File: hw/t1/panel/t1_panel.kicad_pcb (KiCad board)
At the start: 4 copper layers, 70.5 x 81 mm, 391 parts, among them J1 SFP edge (INF-8074i), J2 Rosenberger E6S20A-40MT5-Z (H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, U1 DP83TG720S-Q1 (or DP83TC812S-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, U2 STM32G031F6P6, U3 TPS62822DLC, U4 TPS22918DBVR, Y1 25MHz CL8pF 2016

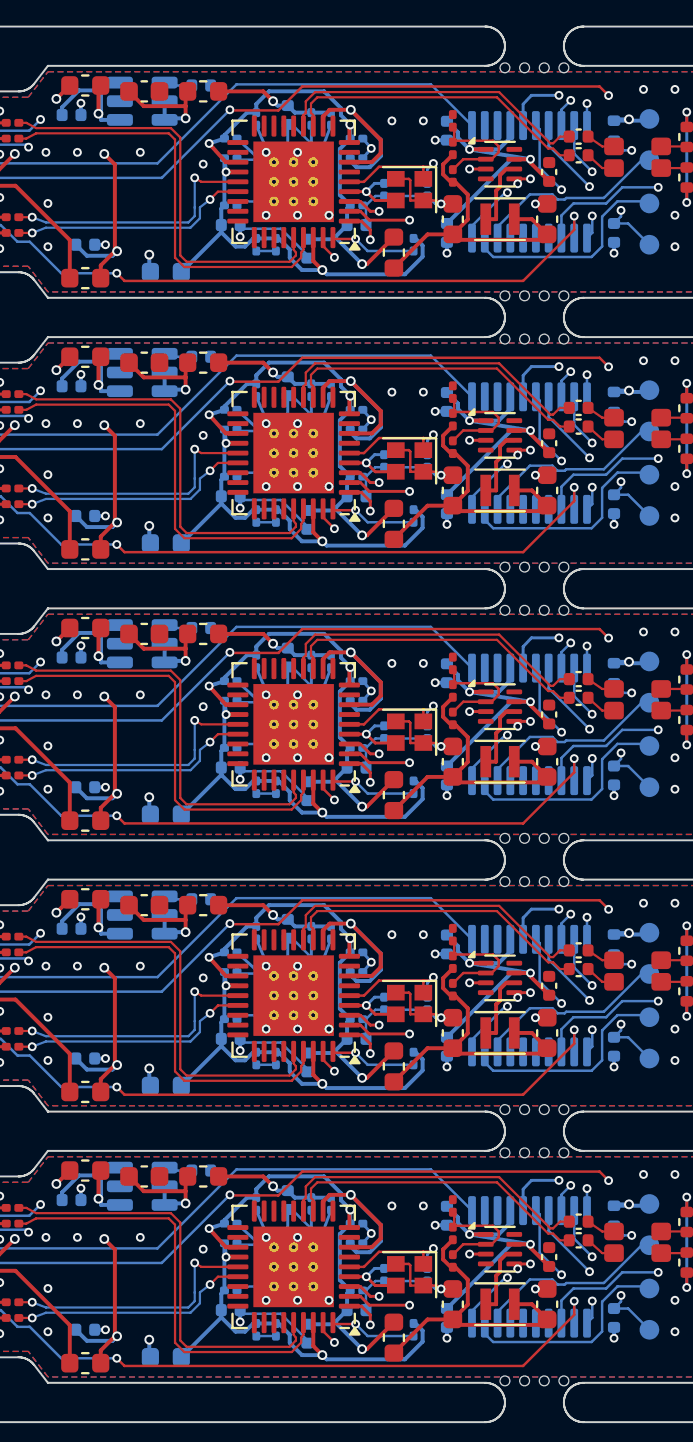
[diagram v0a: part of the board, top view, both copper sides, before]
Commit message: References checked against the design; the fixes they turned up
docs/REFERENCES.md: the standards, Linux drivers, TI / Realtek / Microchip /
Gowin datasheets, app notes and EVMs, and commercial modules, each with a
table of the design against it.

Fixed from it:
- T1S: CLKHOLD_N (K3) tied high - pulled down during configuration, it would
  have held the flash clock and the FPGA would never load; P1 (also
  SSPI_CS_N) pulled up (R26); AN1718 BIN: 0.75 W end-node resistors (were
  0.25 W), 100 V centre cap (was 50 V), no copper under the CMC
- RJ45 / T1S: buck inductor 1.0 uH (TPS6282x Table 3): the RTL8221B wants
  its core switcher out of pulse skipping, which now starts at ~0.15 A, not
  ~0.33 A
- T1: no copper under the CMC on F/In1 (DP83TG720 8.5); the TC812 loadout
  fits the 200 uH CMC its datasheet asks for
- fw: PHY settings 70 ms after reset release (TG720: 65 ms before the first
  MDIO frame) with the 0x56 bridge answering 0xFFFF until then; LAN8670 set-up
  picked by silicon revision (AN1699 Rev G: C2 or D0); collision detection
  follows PLCA as AN1699 asks

All three boards: DRC 0 / 0 unconnected, KiCad 9 PASS, panels clean.
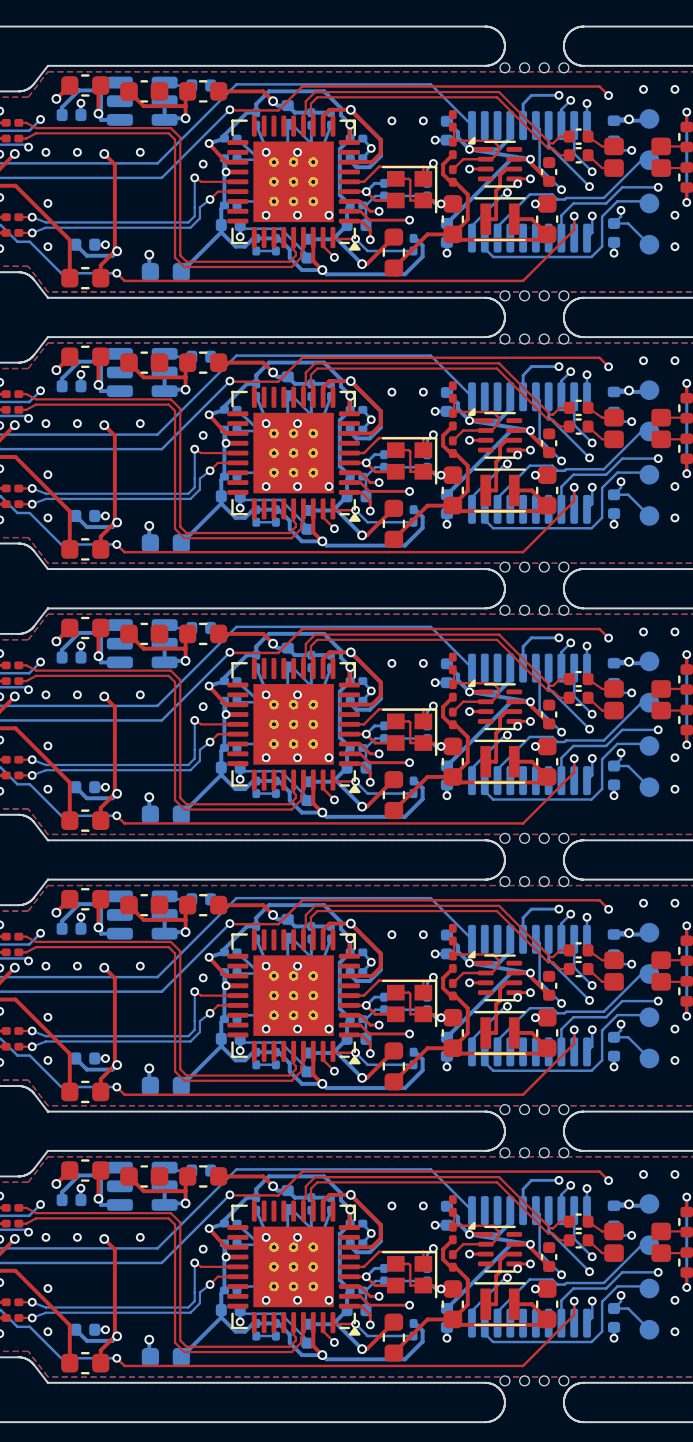
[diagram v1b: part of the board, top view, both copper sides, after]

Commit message: Review fixes: 100 V MDI DC block, 128 Mbit flash, T1S MDI geometry
- T1 C33/C34: 100 nF 100 V X5R 0402 (GRM155R62A104KE14D, C162178), split
  from the 16 V decap line (C1525) they had been grouped with
- T1 R6/R7: 1 k 1 % 0.2 W anti-surge 0402 (C313354) instead of 62.5 mW;
  still short of TI's 0.75 W 2010, documented
- T1S U2: GD25Q128EWIGR (C2982923), same WSON-8 footprint, so Gowin's
  default golden address 0x800000 is inside the part; ORDER.md gives the
  flash layout
- compliance.py: each lane's geometry comes from its routed track width;
  the T1S MDI is two 0.2 mm lines (Z0 44.8) with its own delay and loss,
  and an unsolved width now stops the run
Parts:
- C33 (x5), C34 (x5): value 100nF -> 100nF 100V
- R6 (x5), R7 (x5): value 1k 1% -> 1k 1% 0.2W

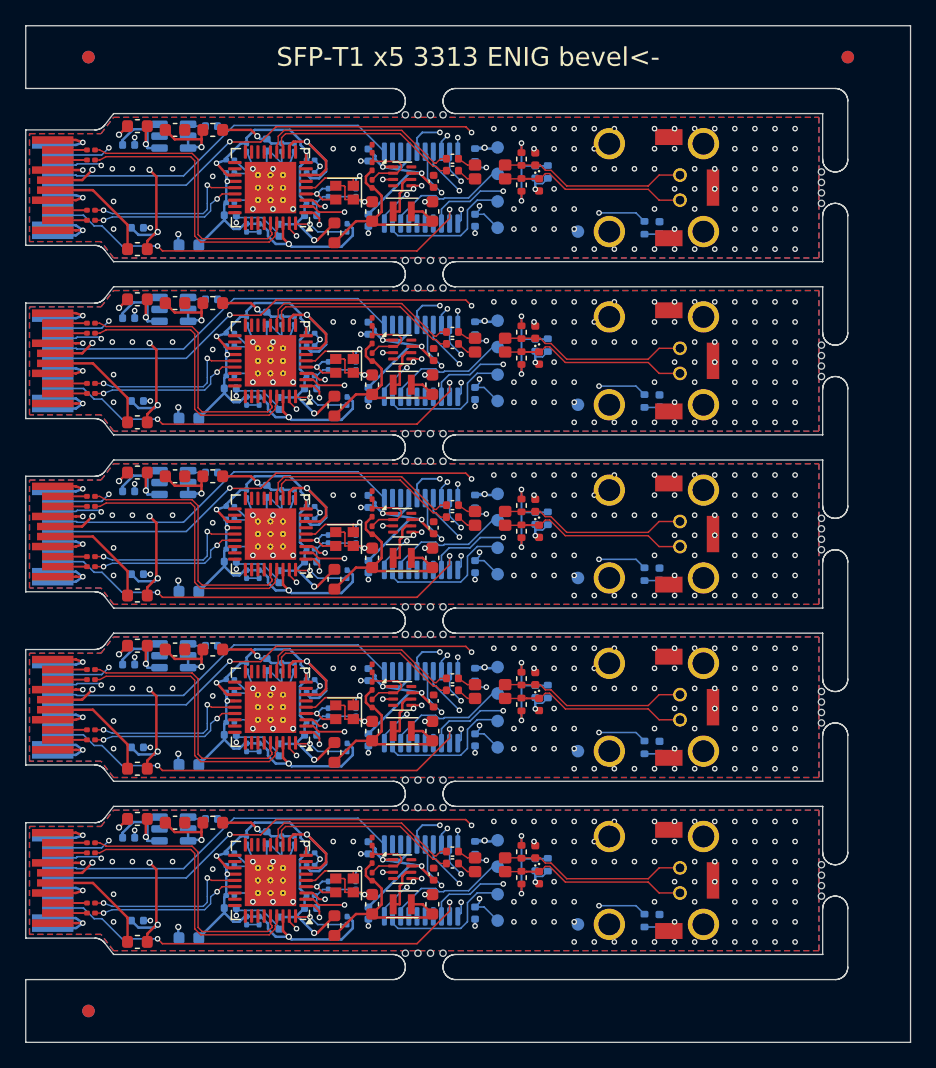
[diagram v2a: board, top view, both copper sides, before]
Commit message: SFP edge was mirrored: fix the pad order, re-lay T1
The edge footprint put pin 20 at the top seen from above with the card edge
on the left; SFF-8419 Figure 7-2 (and INF-8074i Figure 2, drawn the other
way round) has pin 11 there. Every host contact would have landed between
two pads, VccT against ground. pad_y() is negated, the ground-finger vias
follow, and tools/compliance.py now states the expected positions itself.

T1, re-laid on the corrected edge:
- TD reaches the PHY's TX pins and RD its RX pins straight, P to P, both on
  top; the SGMII polarity-invert bits the firmware used to set are gone
- DP83TG720 EP 3.7 mm (RHA0036A), not 4.1
- XI series resistor R9: 0 ohm for the DP83TG720, 100 ohm in the DP83TC812
  loadout (SNLS654D Table 5-1)
- firmware clears SGMII AN on the DP83TC812 (SNLS654D 7.4.12.4)

Shared footprints: CMC land to TDK ACT1210E / Murata DLW32MH (1.05 x 0.6
pads, 0.4 between lines, 2.0 inner gap), H-MTD front solder area 2.2 wide
(MB_633), board thickness 1.0 mm in the files.

RJ45 and T1S still carry the mirrored edge; the README says not to order.
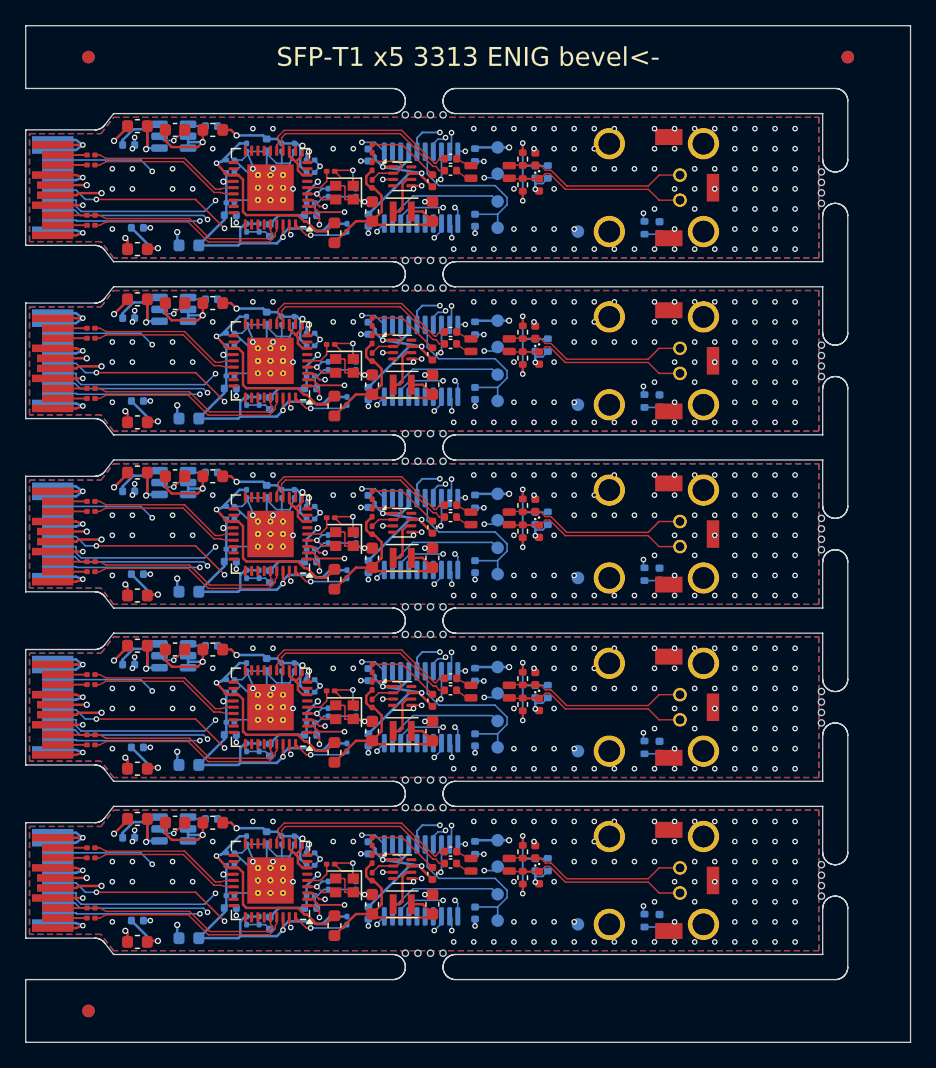
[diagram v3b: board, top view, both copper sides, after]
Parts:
- removed the C21 at (133.4, 50.1)
- removed the C21 at (133.4, 77.7)
- removed the C21 at (133.4, 63.9)
- removed the C21 at (133.4, 91.5)
- removed the C21 at (133.4, 36.3)
- removed the C26 at (145.8, 46.2)
- removed the C26 at (145.8, 73.8)
- removed the C26 at (145.8, 87.6)
- removed the C26 at (145.8, 60.0)
- removed the C26 at (145.8, 32.4)
- removed the C3 at (118.5, 72.1)
- removed the C3 at (118.5, 58.3)
- removed the C3 at (118.5, 44.5)
- removed the C3 at (118.5, 30.7)
- removed the C3 at (118.5, 85.9)
- removed the C33 at (147.2, 44.4)
- removed the C33 at (147.2, 72.0)
- removed the C33 at (147.2, 30.6)
- removed the C33 at (147.2, 58.2)
- removed the C33 at (147.2, 85.8)
- removed the C34 at (147.2, 86.8)
- removed the C34 at (147.2, 31.6)
- removed the C34 at (147.2, 59.1)
- removed the C34 at (147.2, 45.4)
- removed the C34 at (147.2, 73.0)
- removed the C4 at (118.5, 29.9)
- removed the C4 at (118.5, 57.5)
- removed the C4 at (118.5, 71.3)
- removed the C4 at (118.5, 43.7)
- removed the C4 at (118.5, 85.1)
- removed the C5 at (118.5, 62.3)
- removed the C5 at (118.5, 48.5)
- removed the C5 at (118.5, 89.9)
- removed the C5 at (118.5, 34.7)
- removed the C5 at (118.5, 76.1)
- removed the C6 at (118.5, 90.7)
- removed the C6 at (118.5, 49.3)
- removed the C6 at (118.5, 63.1)
- removed the C6 at (118.5, 76.9)
- removed the C6 at (118.5, 35.5)
- removed the FB1 at (122.2, 55.6)
- removed the FB1 at (122.2, 83.2)
- removed the FB1 at (122.2, 28.0)
- removed the FB1 at (122.2, 69.4)
- removed the FB1 at (122.2, 41.8)
- removed the FB2 at (122.2, 93.0)
- removed the FB2 at (122.2, 51.6)
- removed the FB2 at (122.2, 79.2)
- removed the FB2 at (122.2, 37.8)
- removed the FB2 at (122.2, 65.4)
- removed the R6 at (152.8, 85.8)
- removed the R6 at (152.8, 72.0)
- removed the R6 at (152.8, 58.2)
- removed the R6 at (152.8, 44.4)
- removed the R6 at (152.8, 30.6)
- removed the R7 at (152.8, 87.9)
- removed the R7 at (152.8, 74.1)
- removed the R7 at (152.8, 60.3)
- removed the R7 at (152.8, 46.5)
- removed the R7 at (152.8, 32.7)
- removed the U1 at (132.8, 32.9)
- removed the U1 at (132.8, 74.3)
- removed the U1 at (132.8, 46.7)
- removed the U1 at (132.8, 60.5)
- removed the U1 at (132.8, 88.1)
- added C21: 2.2uF, Capacitor_SMD:C_0402_1005Metric, B.Cu at (132.7, 50.1)
- added C21: 2.2uF, Capacitor_SMD:C_0402_1005Metric, B.Cu at (132.7, 91.5)
- added C21: 2.2uF, Capacitor_SMD:C_0402_1005Metric, B.Cu at (132.7, 63.9)
- added C21: 2.2uF, Capacitor_SMD:C_0402_1005Metric, B.Cu at (132.7, 36.3)
- added C21: 2.2uF, Capacitor_SMD:C_0402_1005Metric, B.Cu at (132.7, 77.7)
- added C26: 4.7uF, Capacitor_SMD:C_0402_1005Metric, F.Cu at (145.7, 60.0)
- added C26: 4.7uF, Capacitor_SMD:C_0402_1005Metric, F.Cu at (145.7, 32.4)
- added C26: 4.7uF, Capacitor_SMD:C_0402_1005Metric, F.Cu at (145.7, 87.5)
- added C26: 4.7uF, Capacitor_SMD:C_0402_1005Metric, F.Cu at (145.7, 46.1)
- added C26: 4.7uF, Capacitor_SMD:C_0402_1005Metric, F.Cu at (145.7, 73.8)
- added C3: 100nF, Capacitor_SMD:C_0201_0603Metric, F.Cu at (118.5, 62.7)
- added C3: 100nF, Capacitor_SMD:C_0201_0603Metric, F.Cu at (118.5, 35.1)
- added C3: 100nF, Capacitor_SMD:C_0201_0603Metric, F.Cu at (118.5, 48.9)
- added C3: 100nF, Capacitor_SMD:C_0201_0603Metric, F.Cu at (118.5, 90.3)
- added C3: 100nF, Capacitor_SMD:C_0201_0603Metric, F.Cu at (118.5, 76.5)
- added C33: 100nF 100V, Capacitor_SMD:C_0402_1005Metric, F.Cu at (147.1, 85.8)
- added C33: 100nF 100V, Capacitor_SMD:C_0402_1005Metric, F.Cu at (147.1, 44.4)
- added C33: 100nF 100V, Capacitor_SMD:C_0402_1005Metric, F.Cu at (147.1, 72.0)
- added C33: 100nF 100V, Capacitor_SMD:C_0402_1005Metric, F.Cu at (147.1, 58.2)
- added C33: 100nF 100V, Capacitor_SMD:C_0402_1005Metric, F.Cu at (147.1, 30.6)
- added C34: 100nF 100V, Capacitor_SMD:C_0402_1005Metric, F.Cu at (147.1, 73.0)
- added C34: 100nF 100V, Capacitor_SMD:C_0402_1005Metric, F.Cu at (147.1, 31.6)
- added C34: 100nF 100V, Capacitor_SMD:C_0402_1005Metric, F.Cu at (147.1, 86.8)
- added C34: 100nF 100V, Capacitor_SMD:C_0402_1005Metric, F.Cu at (147.1, 59.1)
- added C34: 100nF 100V, Capacitor_SMD:C_0402_1005Metric, F.Cu at (147.1, 45.4)
- added C4: 100nF, Capacitor_SMD:C_0201_0603Metric, F.Cu at (118.5, 35.9)
- added C4: 100nF, Capacitor_SMD:C_0201_0603Metric, F.Cu at (118.5, 49.7)
- added C4: 100nF, Capacitor_SMD:C_0201_0603Metric, F.Cu at (118.5, 77.3)
- added C4: 100nF, Capacitor_SMD:C_0201_0603Metric, F.Cu at (118.5, 91.1)
- added C4: 100nF, Capacitor_SMD:C_0201_0603Metric, F.Cu at (118.5, 63.5)
- added C5: 100nF, Capacitor_SMD:C_0201_0603Metric, F.Cu at (118.5, 72.5)
- added C5: 100nF, Capacitor_SMD:C_0201_0603Metric, F.Cu at (118.5, 31.1)
- added C5: 100nF, Capacitor_SMD:C_0201_0603Metric, F.Cu at (118.5, 58.7)
- added C5: 100nF, Capacitor_SMD:C_0201_0603Metric, F.Cu at (118.5, 44.9)
- added C5: 100nF, Capacitor_SMD:C_0201_0603Metric, F.Cu at (118.5, 86.3)
- added C6: 100nF, Capacitor_SMD:C_0201_0603Metric, F.Cu at (118.5, 30.3)
- added C6: 100nF, Capacitor_SMD:C_0201_0603Metric, F.Cu at (118.5, 44.1)
- added C6: 100nF, Capacitor_SMD:C_0201_0603Metric, F.Cu at (118.5, 71.7)
- added C6: 100nF, Capacitor_SMD:C_0201_0603Metric, F.Cu at (118.5, 57.9)
- added C6: 100nF, Capacitor_SMD:C_0201_0603Metric, F.Cu at (118.5, 85.5)
- added FB1: BLM18KG601SH1, Inductor_SMD:L_0603_1608Metric, F.Cu at (122.2, 93.0)
- added FB1: BLM18KG601SH1, Inductor_SMD:L_0603_1608Metric, F.Cu at (122.2, 51.6)
- added FB1: BLM18KG601SH1, Inductor_SMD:L_0603_1608Metric, F.Cu at (122.2, 65.4)
- added FB1: BLM18KG601SH1, Inductor_SMD:L_0603_1608Metric, F.Cu at (122.2, 37.8)
- added FB1: BLM18KG601SH1, Inductor_SMD:L_0603_1608Metric, F.Cu at (122.2, 79.2)
- added FB2: BLM18KG601SH1, Inductor_SMD:L_0603_1608Metric, F.Cu at (122.2, 28.0)
- added FB2: BLM18KG601SH1, Inductor_SMD:L_0603_1608Metric, F.Cu at (122.2, 55.6)
- added FB2: BLM18KG601SH1, Inductor_SMD:L_0603_1608Metric, F.Cu at (122.2, 41.8)
- added FB2: BLM18KG601SH1, Inductor_SMD:L_0603_1608Metric, F.Cu at (122.2, 69.4)
- added FB2: BLM18KG601SH1, Inductor_SMD:L_0603_1608Metric, F.Cu at (122.2, 83.2)
- added R6: 1k 1% 0.2W, Resistor_SMD:R_0402_1005Metric, F.Cu at (152.8, 58.2)
- added R6: 1k 1% 0.2W, Resistor_SMD:R_0402_1005Metric, F.Cu at (152.8, 85.8)
- added R6: 1k 1% 0.2W, Resistor_SMD:R_0402_1005Metric, F.Cu at (152.8, 44.4)
- added R6: 1k 1% 0.2W, Resistor_SMD:R_0402_1005Metric, F.Cu at (152.8, 30.6)
- added R6: 1k 1% 0.2W, Resistor_SMD:R_0402_1005Metric, F.Cu at (152.8, 72.0)
- added R7: 1k 1% 0.2W, Resistor_SMD:R_0402_1005Metric, F.Cu at (152.8, 74.1)
- added R7: 1k 1% 0.2W, Resistor_SMD:R_0402_1005Metric, F.Cu at (152.8, 32.7)
- added R7: 1k 1% 0.2W, Resistor_SMD:R_0402_1005Metric, F.Cu at (152.8, 60.3)
- added R7: 1k 1% 0.2W, Resistor_SMD:R_0402_1005Metric, F.Cu at (152.8, 46.5)
- added R7: 1k 1% 0.2W, Resistor_SMD:R_0402_1005Metric, F.Cu at (152.8, 87.9)
- added R9: 0, Resistor_SMD:R_0201_0603Metric, F.Cu at (137.6, 45.4)
- added R9: 0, Resistor_SMD:R_0201_0603Metric, F.Cu at (137.6, 73.0)
- added R9: 0, Resistor_SMD:R_0201_0603Metric, F.Cu at (137.6, 86.8)
- added R9: 0, Resistor_SMD:R_0201_0603Metric, F.Cu at (137.6, 31.6)
- added R9: 0, Resistor_SMD:R_0201_0603Metric, F.Cu at (137.6, 59.2)
- added U1: DP83TG720S-Q1 (or DP83TC812S-Q1), Package_DFN_QFN:QFN-36-1EP_6x6mm_P0.5mm_EP3.7x3.7mm_ThermalVias, F.Cu at (132.8, 88.1)
- added U1: DP83TG720S-Q1 (or DP83TC812S-Q1), Package_DFN_QFN:QFN-36-1EP_6x6mm_P0.5mm_EP3.7x3.7mm_ThermalVias, F.Cu at (132.8, 46.7)
- added U1: DP83TG720S-Q1 (or DP83TC812S-Q1), Package_DFN_QFN:QFN-36-1EP_6x6mm_P0.5mm_EP3.7x3.7mm_ThermalVias, F.Cu at (132.8, 60.5)
- added U1: DP83TG720S-Q1 (or DP83TC812S-Q1), Package_DFN_QFN:QFN-36-1EP_6x6mm_P0.5mm_EP3.7x3.7mm_ThermalVias, F.Cu at (132.8, 74.3)
- added U1: DP83TG720S-Q1 (or DP83TC812S-Q1), Package_DFN_QFN:QFN-36-1EP_6x6mm_P0.5mm_EP3.7x3.7mm_ThermalVias, F.Cu at (132.8, 32.9)
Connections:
- net Board_0-XI renamed Board_0-XI_X
- net Board_1-XI renamed Board_1-XI_X
- net Board_2-XI renamed Board_2-XI_X
- net Board_3-XI renamed Board_3-XI_X
- net Board_4-XI renamed Board_4-XI_X
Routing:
- net Board_1-SCL: track 48.8 -> 28.3 mm
- net Board_4-SCL: track 48.8 -> 28.3 mm
- net Board_0-SCL: track 48.8 -> 28.3 mm
- net Board_2-SCL: track 48.8 -> 28.3 mm
- net Board_3-SCL: track 48.8 -> 28.3 mm
- net Board_4-TX_FAULT: track 47.0 -> 32.6 mm
- net Board_0-TX_FAULT: track 47.0 -> 32.6 mm
- net Board_1-TX_FAULT: track 47.0 -> 32.6 mm
- net Board_3-TX_FAULT: track 47.0 -> 32.6 mm
- net Board_2-TX_FAULT: track 47.0 -> 32.6 mm
- net Board_4-VDD1P0: track 24.4 -> 36.0 mm
- net Board_1-VDD1P0: track 24.4 -> 36.0 mm
- net Board_3-VDD1P0: track 24.4 -> 36.0 mm
- net Board_2-VDD1P0: track 24.4 -> 36.0 mm
- net Board_0-VDD1P0: track 24.4 -> 36.0 mm
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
